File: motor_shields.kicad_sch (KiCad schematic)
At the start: 42 parts, among them IC1 BTN70301EPAXUMA1, IC2 BTN70301EPAXUMA1, IC3 BTN70301EPAXUMA1, IC4 BTN70301EPAXUMA1, IC6 BTN70301EPAXUMA1, IC8 BTN70301EPAXUMA1, J4 Conn_01x06_Pin, J5 Conn_01x06_Pin, J8 Conn_01x06_Pin

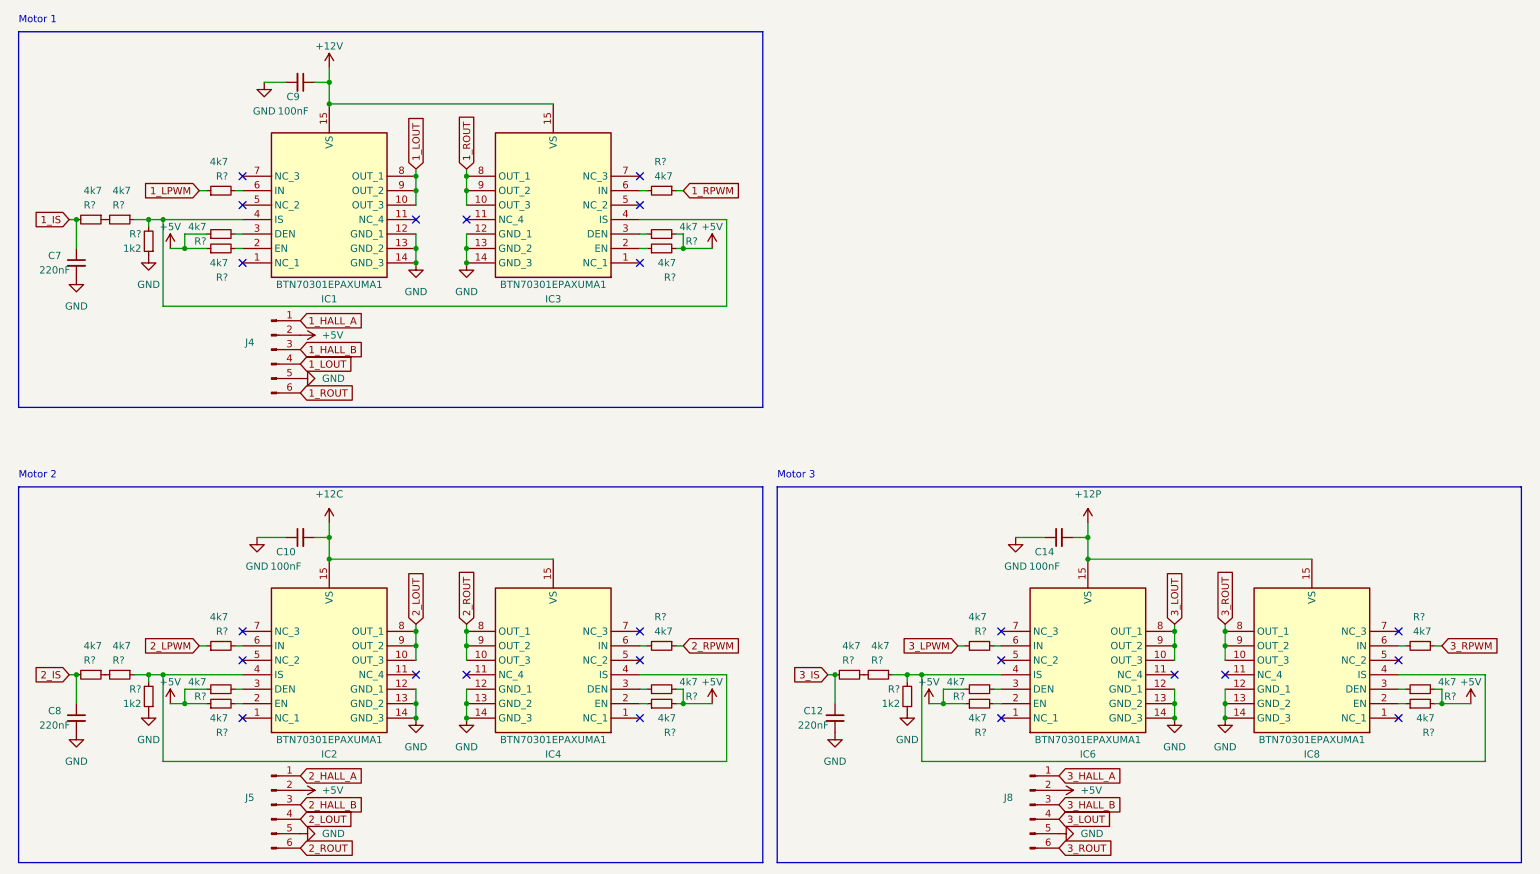
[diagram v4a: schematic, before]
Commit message: Completed full schematics
New features:
- extra 5V reg for handling camera current
- extra 12V reg for powering external LEDs
- added circuit for external emergency stop switch
- added some solder jumper for design flexibility
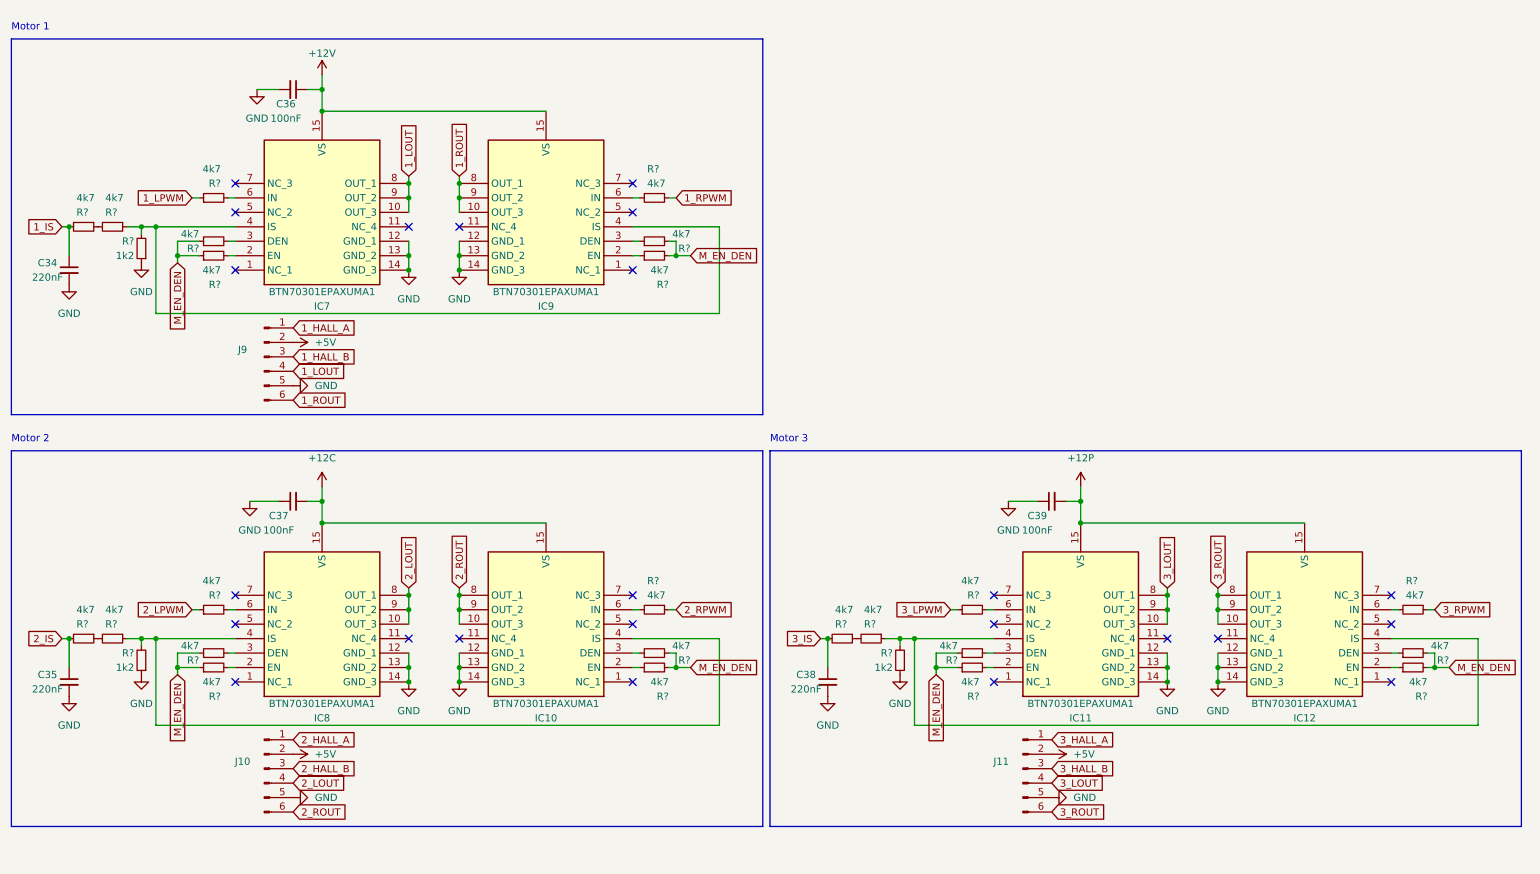
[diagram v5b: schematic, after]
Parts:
- renumbered C7 to C34, C8 to C35, C9 to C36, C10 to C37, C12 to C38, C14 to C39, IC4 to IC10, IC6 to IC11, IC8 to IC12, IC1 to IC7, IC2 to IC8, IC3 to IC9, J5 to J10, J8 to J11, J4 to J9
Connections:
- net +5V: no longer R?.1, R?.1, R?.1, R?.1, R?.1, R?.1, R?.2, R?.2, R?.2, R?.2, R?.2, R?.2
- new net M_EN_DEN: R?.1, R?.1, R?.1, R?.1, R?.1, R?.1, R?.2, R?.2, R?.2, R?.2, R?.2, R?.2
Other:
- moved on the sheet: C34, C35, C36, C37, C38, C39, IC10, IC11, IC12, IC7, IC8, IC9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

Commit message: footprint assignment WIP
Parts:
- renumbered C34 to C28, C35 to C29, C36 to C30, C37 to C31, C38 to C32, C39 to C33, IC11 to IC10, IC12 to IC11, IC7 to IC6, IC8 to IC7, IC9 to IC8, IC10 to IC9, J9 to J10, J10 to J11, J11 to J12

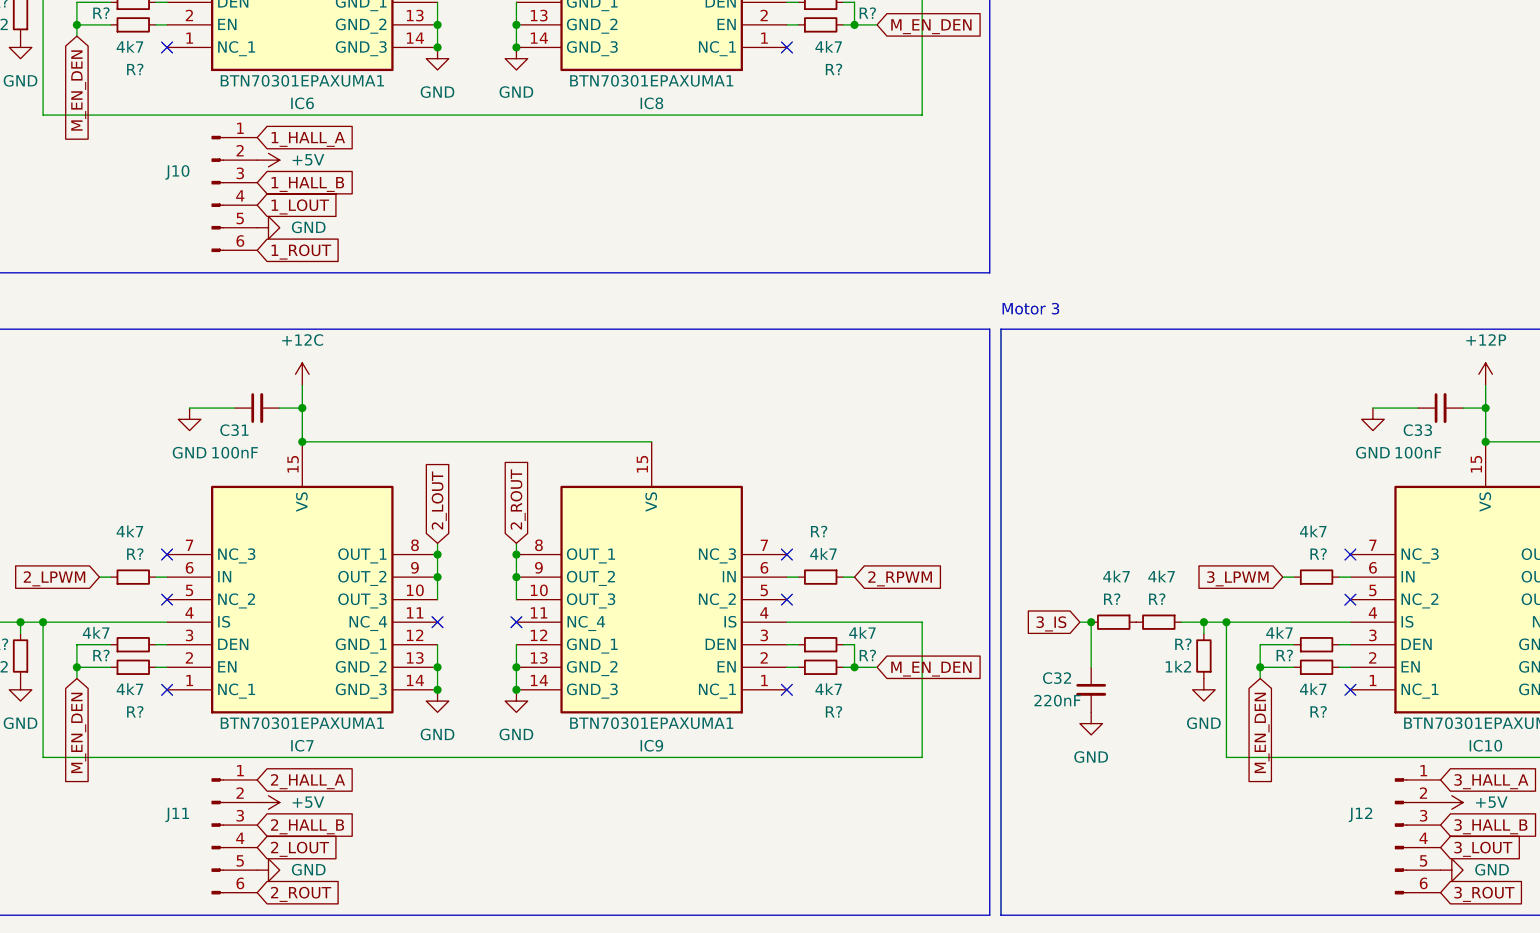
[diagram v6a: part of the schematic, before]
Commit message: completed footprint assignments
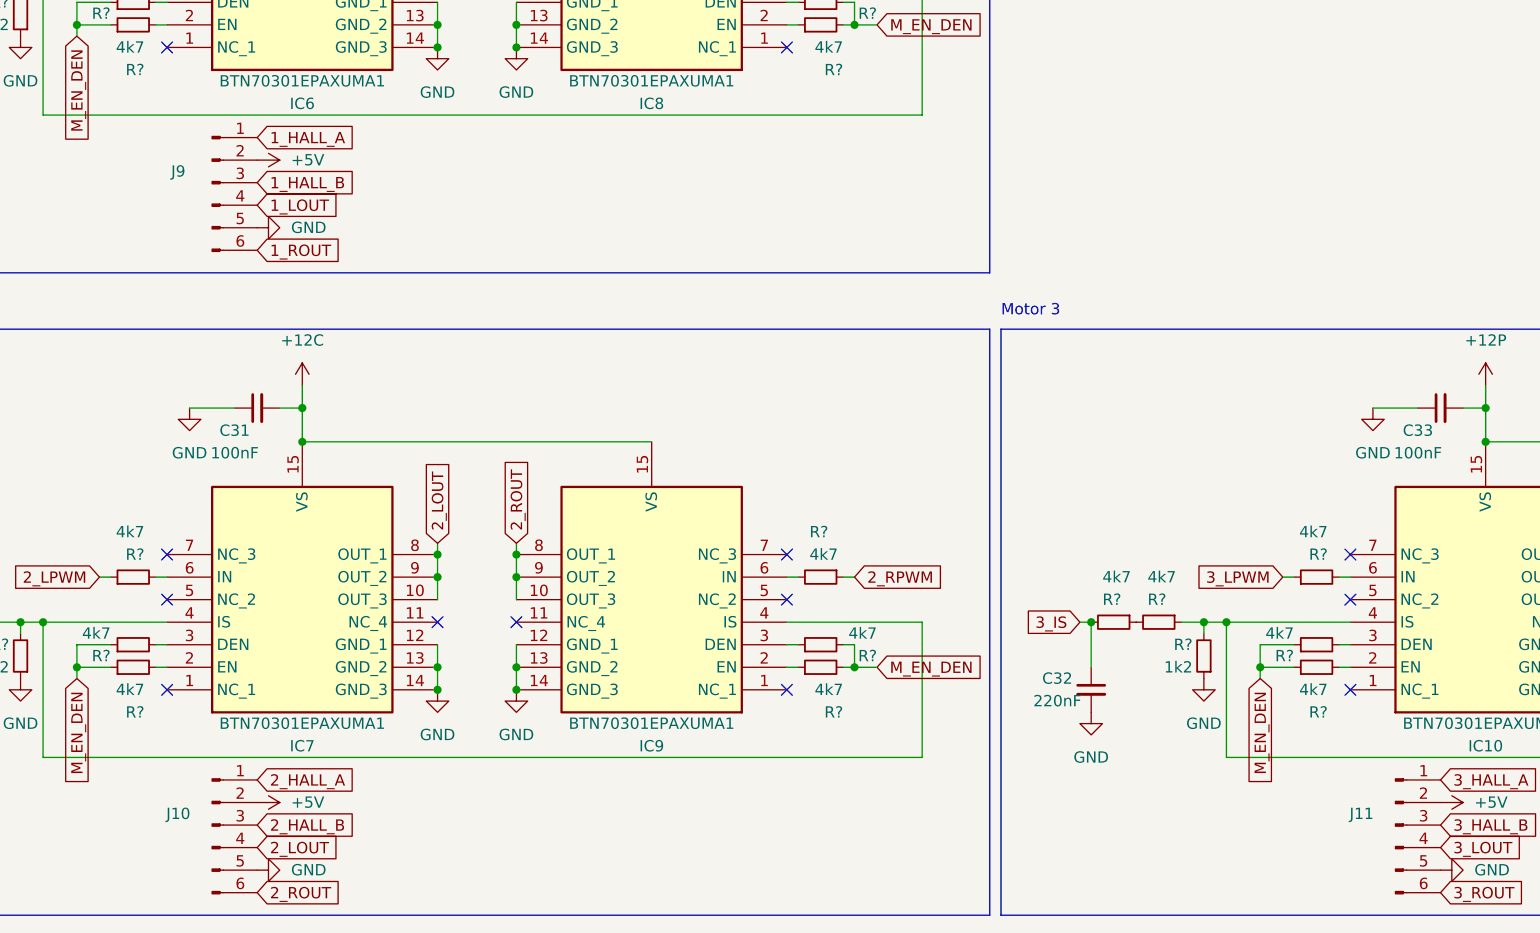
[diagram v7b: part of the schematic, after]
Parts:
- C28, C29, C32: footprint Capacitor_SMD:C_0402_1005Metric_Pad0.74x0.62mm_HandSolder -> Capacitor_SMD:C_0805_2012Metric
- C30, C31, C33: footprint Capacitor_SMD:C_0603_1608Metric_Pad1.08x0.95mm_HandSolder -> Capacitor_SMD:C_0402_1005Metric
- R? (x27): footprint Resistor_SMD:R_1206_3216Metric_Pad1.30x1.75mm_HandSolder -> Resistor_SMD:R_1206_3216Metric
- renumbered J11 to J10, J12 to J11, J10 to J9
